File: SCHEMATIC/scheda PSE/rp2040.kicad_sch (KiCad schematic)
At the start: 25 parts

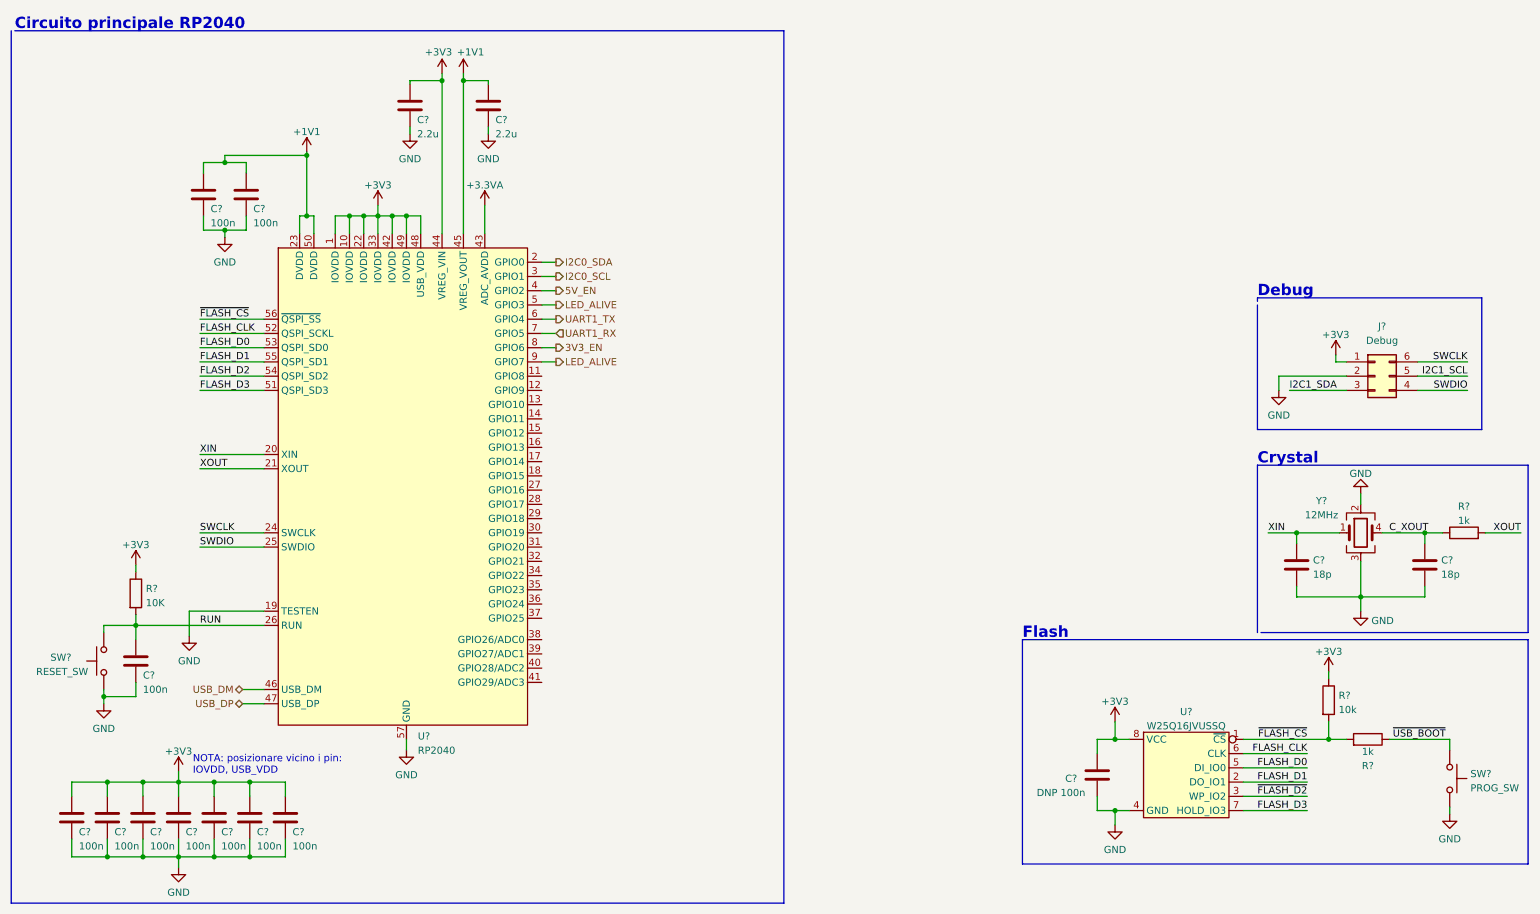
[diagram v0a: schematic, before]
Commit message: sistemato tutto, e aggiunti i footprint da modificare
sistemato tutto, aggiunto e modificato i footprint.
Manca solo aggiungere i restanti footprint (praticamente solo dei componenti comuni)
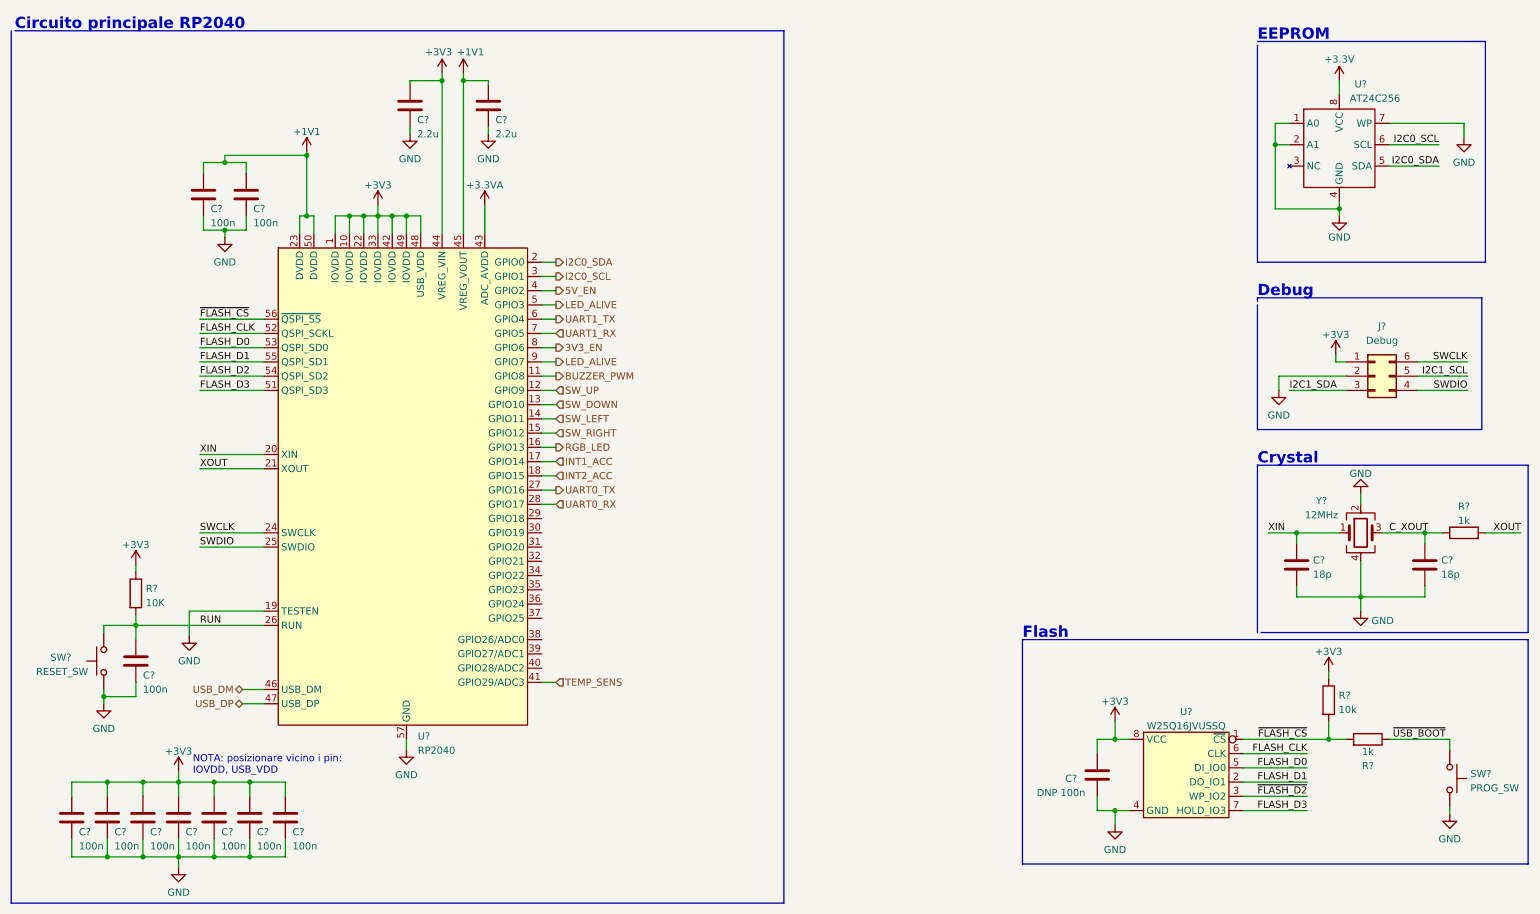
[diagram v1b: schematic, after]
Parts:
- added U?: AT24C256, Package_SO:SOIC-8_3.9x4.9mm_P1.27mm, symbol altro:AT24C256
- Y?: footprint (none) -> Crystal:Crystal_SMD_3225-4Pin_3.2x2.5mm_HandSoldering; symbol Device:Crystal_GND23 -> Device:Crystal_GND24
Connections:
- net C_XOUT: now also Y?.3; no longer Y?.4
- net GND: now also Y?.4, U?.1 (A0), U?.2 (A1), U?.4 (GND), U?.7 (WP); no longer Y?.3
- net I2C0_SCL: now also U?.6 (SCL)
- net I2C0_SDA: now also U?.5 (SDA)
- net BUZZER_PWM: now reaches U?.11 (GPIO8)
- net SW_UP: now reaches U?.12 (GPIO9)
- net SW_DOWN: now reaches U?.13 (GPIO10)
- net SW_LEFT: now reaches U?.14 (GPIO11)
- net SW_RIGHT: now reaches U?.15 (GPIO12)
- net RGB_LED: now reaches U?.16 (GPIO13)
- net INT1_ACC: now reaches U?.17 (GPIO14)
- net INT2_ACC: now reaches U?.18 (GPIO15)
- net UART0_TX: now reaches U?.27 (GPIO16)
- net UART0_RX: now reaches U?.28 (GPIO17)
- net TEMP_SENS: now reaches U?.41 (GPIO29/ADC3)
- new net +3.3V: U?.8 (VCC)
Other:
- note added: "EEPROM"

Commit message: prova librerie
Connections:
- net I2C1_SCL: now also U?.30 (GPIO19)
- net I2C1_SDA: now also U?.29 (GPIO18)

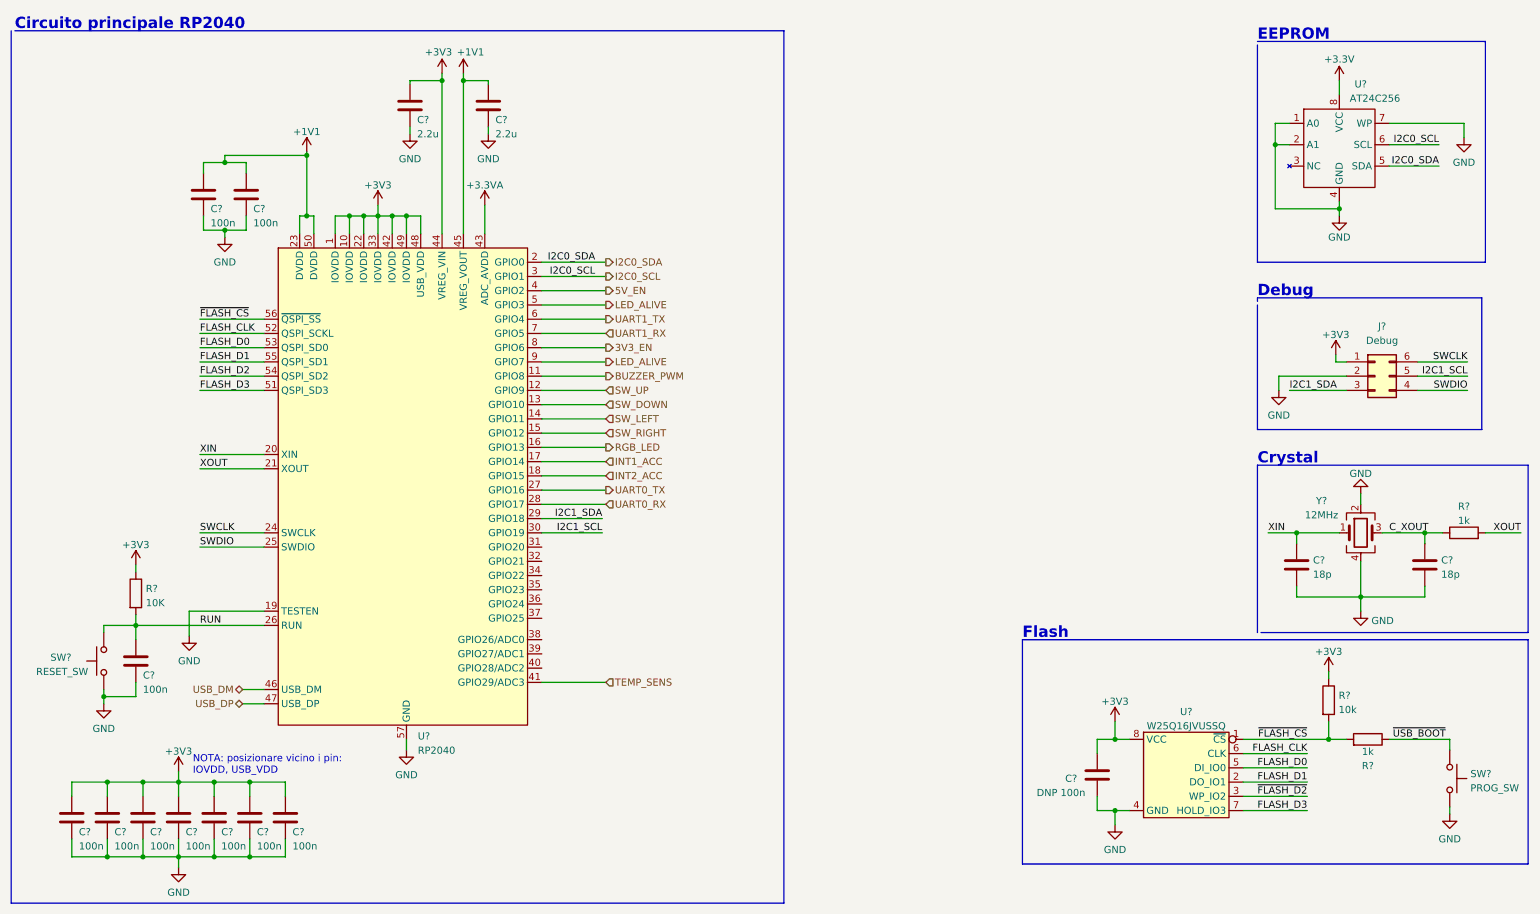
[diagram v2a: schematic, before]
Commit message: Aggiunti QUASI tutti i footprint
aggiunti quasi tutti i footprint dei componenti
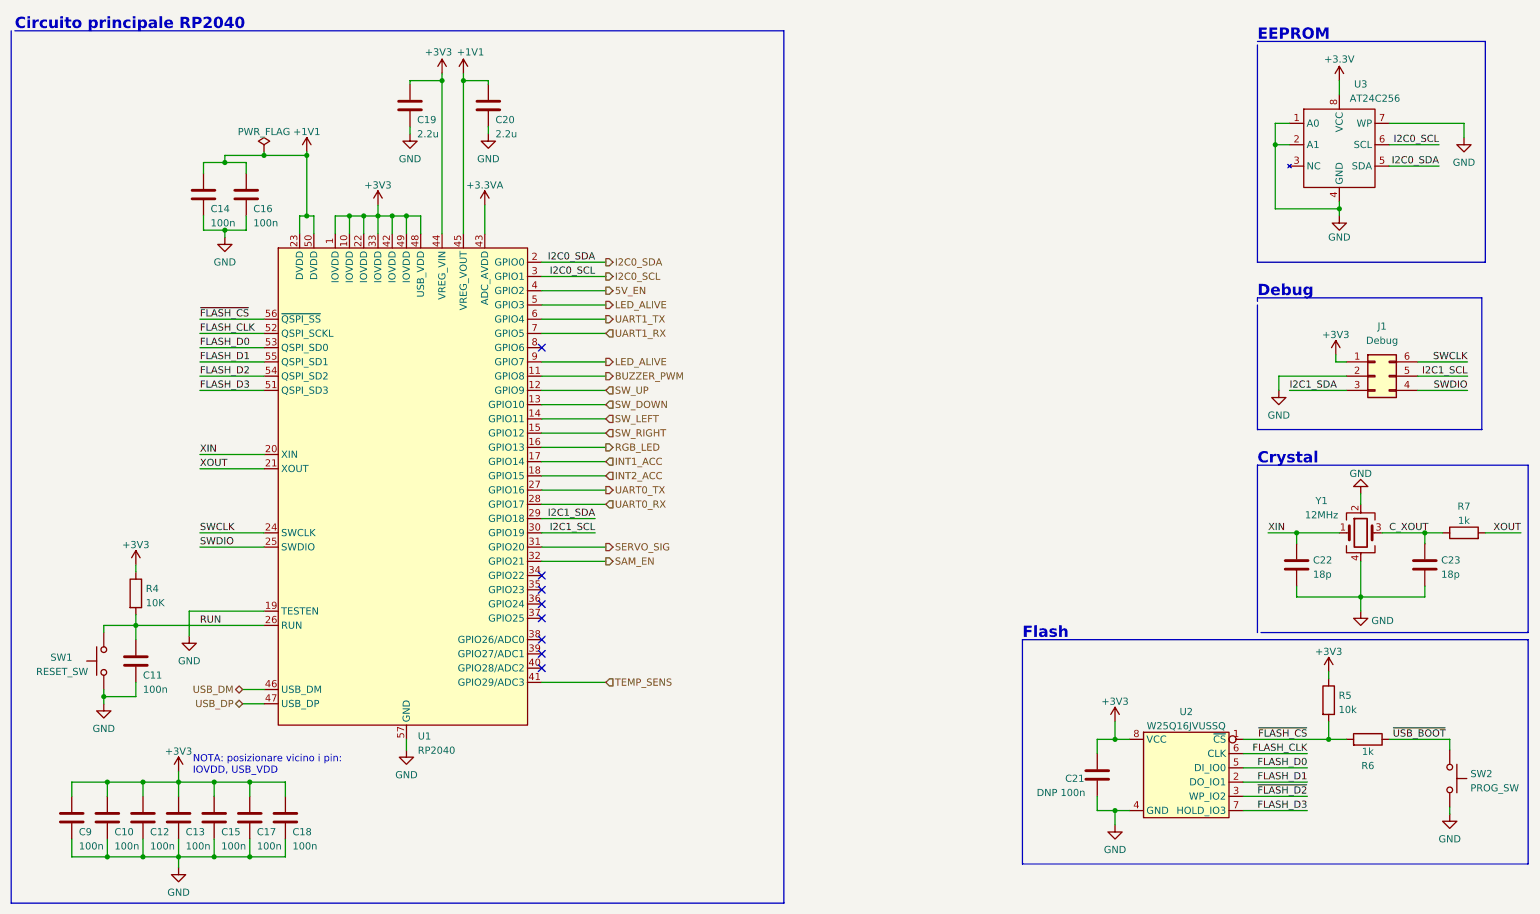
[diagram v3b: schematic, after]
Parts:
- C10, C11, C12, C13, C14, C15, C16, C17, C18, C19, C20, C22, C23, C9: renamed from C?; footprint (none) -> Capacitor_SMD:C_0603_1608Metric
- J1: renamed from J?; footprint (none) -> Connector_PinSocket_2.54mm:PinSocket_2x03_P2.54mm_Vertical
- R4, R5, R6, R7: renamed from R?; footprint (none) -> Resistor_SMD:R_0603_1608Metric
- SW1, SW2: renamed from SW?; footprint (none) -> Button_Switch_THT:SW_PUSH_6mm_H5mm
- gave numbers to parts that had none: 5
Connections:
- net SERVO_SIG: now reaches U1.31 (GPIO20)
- net SAM_EN: now reaches U1.32 (GPIO21)
- net 3V3_EN: no longer names the net of U1.8 (GPIO6)
- no-connect marks 0 -> 8

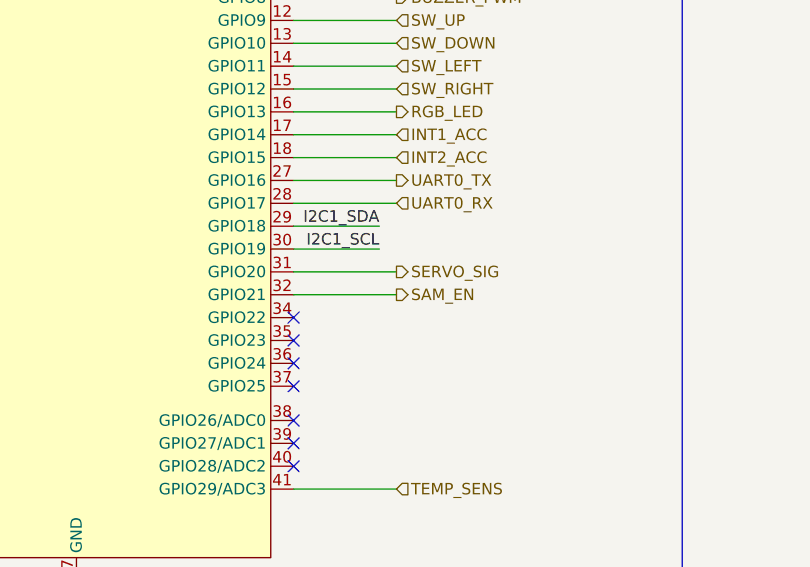
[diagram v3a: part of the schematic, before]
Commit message: iniziato il layout, posizionati componenti principali
incominciato il posizionamento dei componenti nel layout. Sono stati posizionati i componenti principali come led RGB, GPS, schermo, pulsanti vari, buzzer
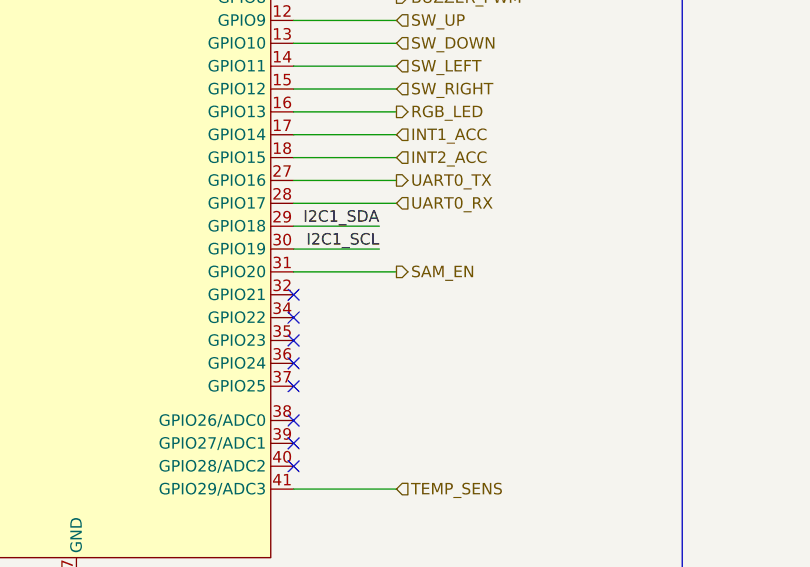
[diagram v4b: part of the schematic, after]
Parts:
- C21: footprint (none) -> Capacitor_SMD:C_0603_1608Metric
- J1: footprint Connector_PinSocket_2.54mm:PinSocket_2x03_P2.54mm_Vertical -> Connector_PinHeader_2.54mm:PinHeader_2x03_P2.54mm_Vertical
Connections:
- net SERVO_SIG is gone; now on net SAM_EN: U1.31 (GPIO20)
- net SAM_EN: no longer U1.32 (GPIO21)
- no-connect marks 8 -> 9
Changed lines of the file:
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@@
   (no_connect (at 107.95 73.025))
   (no_connect (at 107.95 130.175))
+  (no_connect (at 107.95 111.125))
   (no_connect (at 107.95 125.095))
   (no_connect (at 107.95 121.285))
@@
     (stroke (width 0) (type default) (color 0 0 0 0))
   )
-  (wire (pts (xy 107.95 111.125) (xy 119.38 111.125))
+  (wire (pts (xy 107.95 108.585) (xy 119.38 108.585))
     (stroke (width 0) (type default) (color 0 0 0 0))
   )
@@
   )
   (wire (pts (xy 237.49 106.045) (xy 242.57 106.045))
-    (stroke (width 0) (type default) (color 0 0 0 0))
-  )
-  (wire (pts (xy 107.95 108.585) (xy 119.38 108.585))
     (stroke (width 0) (type default) (color 0 0 0 0))
   )
@@
     (effects (font (size 1.27 1.27)) (justify left))
   )
-  (hierarchical_label "SERVO_SIG" (shape output) (at 119.38 108.585 0)
-    (effects (font (size 1.27 1.27)) (justify left))
-  )
   (hierarchical_label "UART1_RX" (shape input) (at 119.38 70.485 0)
     (effects (font (size 1.27 1.27)) (justify left))
@@
     (effects (font (size 1.27 1.27)) (justify left))
   )
-  (hierarchical_label "SAM_EN" (shape output) (at 119.38 111.125 0)
+  (hierarchical_label "SAM_EN" (shape output) (at 119.38 108.585 0)
     (effects (font (size 1.27 1.27)) (justify left))
   )
@@
     (property "Reference" "J1" (id 0) (at 257.81 69.2181 0))
     (property "Value" "Debug" (id 1) (at 257.81 71.755 0))
-    (property "Footprint" "Connector_PinSocket_2.54mm:PinSocket_2x03_P2.54mm_Vertical" (id 2) (at 256.54 78.105 0)
+    (property "Footprint" "Connector_PinHeader_2.54mm:PinHeader_2x03_P2.54mm_Vertical" (id 2) (at 256.54 78.105 0)
       (effects (font (size 1.27 1.27)) hide)
     )
@@
       (effects (font (size 1.27 1.27)) (justify left))
     )
-    (property "Footprint" "" (id 2) (at 207.9752 153.035 0)
-      (effects (font (size 1.27 1.27)) hide)
-    )
+    (property "Footprint" "Capacitor_SMD:C_0603_1608Metric" (id 2) (at 207.9752 153.035 0)
+      (effects (font (size 1.27 1.27)) hide)
+    )
